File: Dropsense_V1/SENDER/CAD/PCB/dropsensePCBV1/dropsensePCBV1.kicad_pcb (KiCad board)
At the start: 2 copper layers, 49.5 x 50 mm, 26 parts, among them J1 Micro_SD_Card_Det_Hirose_DM3AT, J2 USB_B_Micro, J3 battery socket, SW1 SW_Push, SW2 SW_Push, U1 ESP32-S3-WROOM-1, U2 MPU-6050, U3 TP4056-42-ESOP8, U4 ME6211C10M5

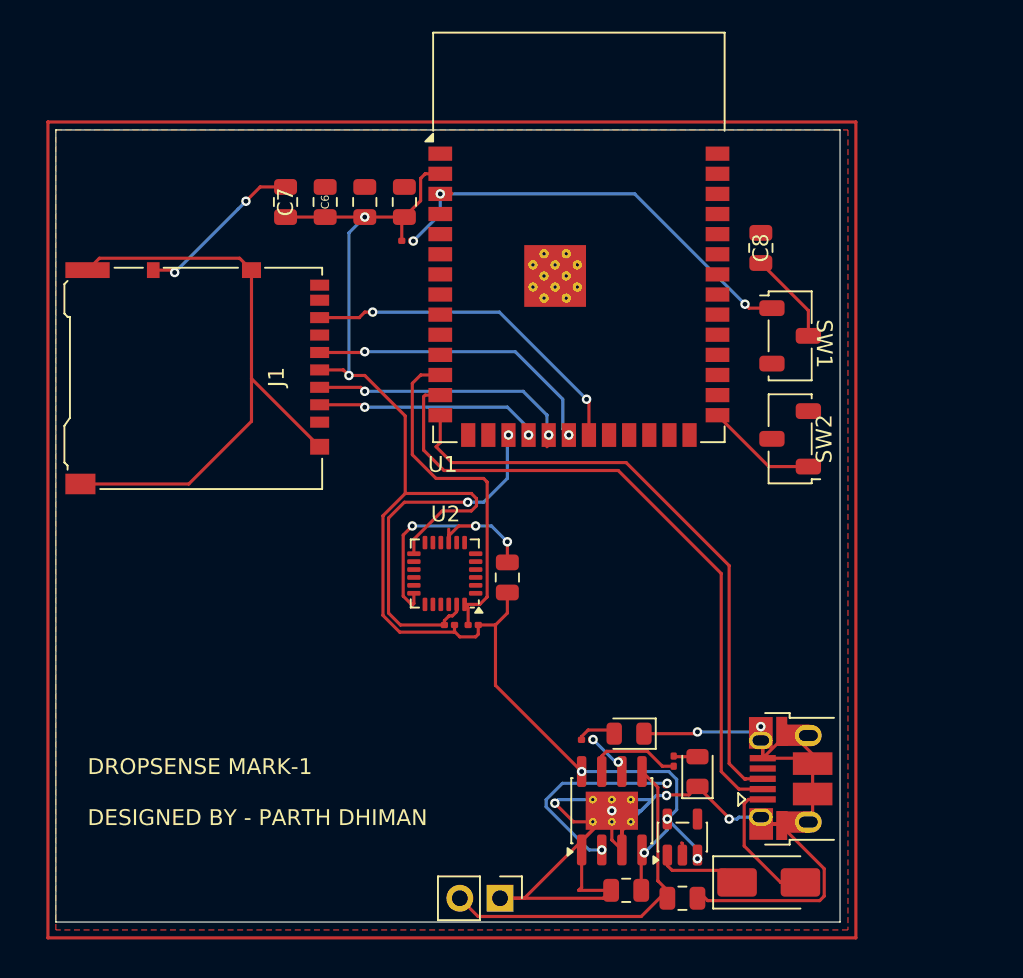
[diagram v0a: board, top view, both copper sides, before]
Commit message: PCB improvement
updated and polished both the pcbs of the sender and reciever mainly woked on moving viases away from smd components
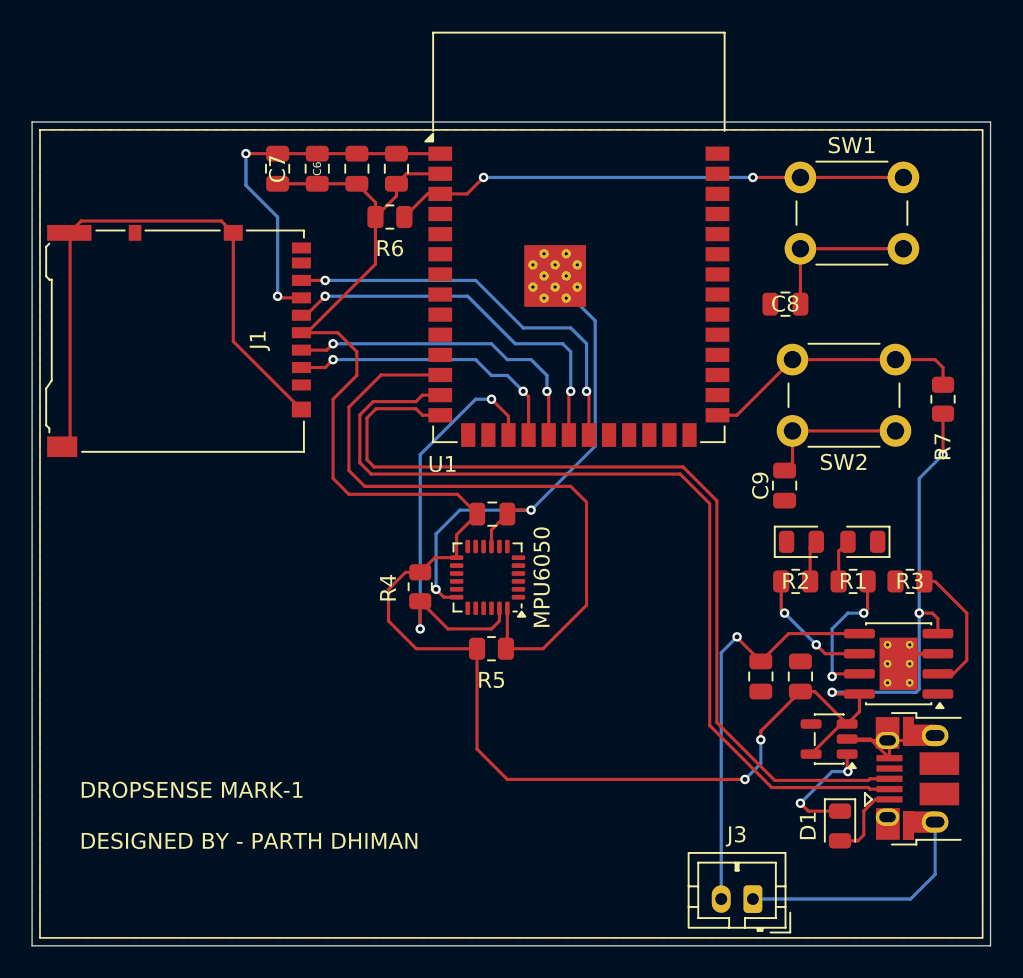
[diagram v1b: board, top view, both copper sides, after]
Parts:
- added C9: 10uF, Capacitor_SMD:C_0805_2012Metric, F.Cu at (125.5, 72.5)
- added R7: 10R, Resistor_SMD:R_0805_2012Metric, F.Cu at (135.5, 67.0)
- D1: footprint Diode_SMD:D_SMA -> Diode_SMD:D_0805_2012Metric
- J3: footprint Connector_PinHeader_2.54mm:PinHeader_1x02_P2.54mm_Vertical -> Connector_JST:JST_PH_B2B-PH-K_1x02_P2.00mm_Vertical
- R1, R2, R3, R4, R5, R6: footprint Resistor_SMD:R_0201_0603Metric -> Resistor_SMD:R_0805_2012Metric
- SW1, SW2: footprint Button_Switch_SMD:Nidec_Copal_CAS-120A -> Button_Switch_THT:SW_PUSH_6mm_H4.3mm
- moved U3 20.3 mm to (132.7, 83.7), turned to 180 degrees
- moved R3 20.3 mm to (133.4, 78.5), turned to 180 degrees
- moved D2 17.9 mm to (130.4, 76.0), turned to 180 degrees
- moved C2 17.4 mm to (126.5, 84.5), turned to 90 degrees
- moved R2 16.6 mm to (126.2, 78.5), turned to 0 degrees
- moved D3 16.3 mm to (126.6, 76.0), turned to 0 degrees
- moved R1 16.0 mm to (129.8, 78.5), turned to 180 degrees
- moved J3 16.0 mm to (123.5, 98.5), turned to 180 degrees
- moved C1 14.8 mm to (124.0, 84.5), turned to -90 degrees
- moved U4 11.1 mm to (128.3, 88.5), turned to 180 degrees
- moved SW1 10.0 mm to (126.5, 53.0)
- moved J2 8.00 mm to (133.9, 90.9)
- moved SW2 6.67 mm to (132.5, 69.0)
- moved D1 5.74 mm to (129.0, 93.9), turned to -90 degrees
- moved C3 4.11 mm to (107.0, 74.2), turned to 180 degrees
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- renumbered U2 to MPU6050
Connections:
- net gpio19 renamed D+
- net gpio20 renamed D-
- SW2 pad 1: IO0 -> Net-(C9-Pad1)
- SW2 pad 2: GND -> IO0
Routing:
- net GND: track 133.3 -> 88.0 mm, vias 11 -> 4
- net 3v3: track 94.7 -> 129.8 mm, vias 6 -> 5
- net SDA: track 22.2 -> 41.7 mm
- net D+: track 38.8 -> 57.3 mm
- net D-: track 42.1 -> 58.8 mm
- net IO0: track 7.08 -> 17.0 mm
- net Net-(C9-Pad1): track 0.00 -> 9.21 mm
- net SCL: track 22.9 -> 28.1 mm
- net SCk: track 19.0 -> 24.3 mm
- net Net-(U3-PROG): track 13.9 -> 8.67 mm, vias 2 -> 0
- net Net-(U3-~{STDBY}): track 2.87 -> 7.88 mm
- net Net-(U1-EN): track 27.8 -> 32.5 mm, vias 3 -> 2
- net Net-(C8-Pad1): track 5.84 -> 10.0 mm
- net MISO: track 21.6 -> 25.5 mm
- net /+ve: track 22.4 -> 26.1 mm, vias 0 -> 1
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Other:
- board size 49.5 x 50 mm -> 60.5 x 52 mm

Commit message: 3d design of sender enclosure started
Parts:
- added G***: LOGO, hackclublogo:hackclublogo, F.Cu at (90.0, 77.0)
- added REF**: MountingHole_2.2mm_M2, MountingHole:MountingHole_2.2mm_M2, F.Cu at (135.0, 98.0)
- added REF**: MountingHole_2.2mm_M2, MountingHole:MountingHole_2.2mm_M2, F.Cu at (81.5, 98.0)
- added REF**: MountingHole_2.2mm_M2, MountingHole:MountingHole_2.2mm_M2, F.Cu at (81.5, 53.0)
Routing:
- net GND: track 88.0 -> 86.1 mm
